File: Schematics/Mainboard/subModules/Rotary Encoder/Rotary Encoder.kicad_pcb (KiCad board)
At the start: 2 copper layers, 22.1 x 22.1 mm, 7 parts, among them J1 Power, J2 Data, SW1 Rot

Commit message: Moved F.Fab
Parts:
- moved R1 16.8 mm to (134.6, 107.7), turned to 90 degrees
- moved J2 16.1 mm to (155.7, 98.9), turned to 0 degrees
- moved J1 16.0 mm to (133.6, 104.0), turned to 180 degrees
- moved R2 14.8 mm to (136.4, 107.7), turned to 90 degrees
- moved R3 14.4 mm to (136.4, 95.0), turned to -90 degrees
- moved C1 11.5 mm to (136.4, 101.3), turned to 90 degrees
- moved SW1 11.3 mm to (142.2, 108.7), turned to 90 degrees

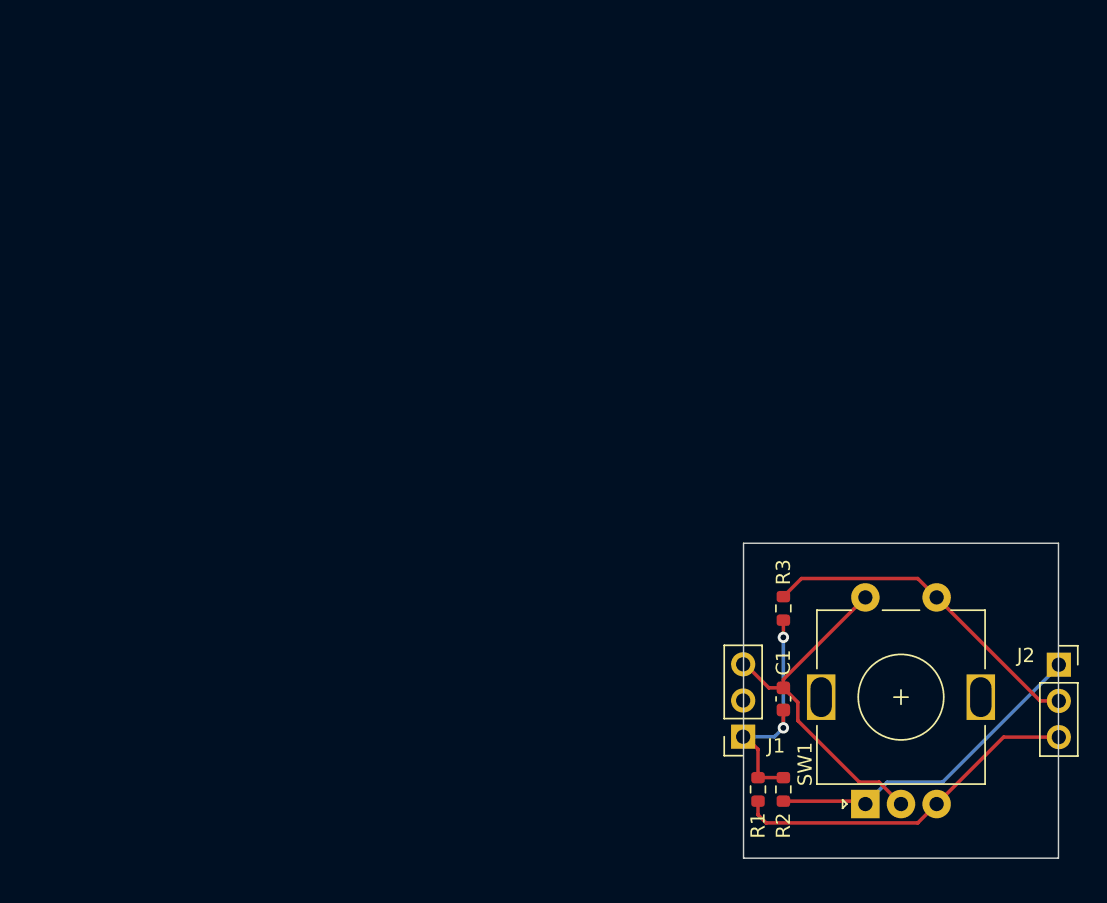
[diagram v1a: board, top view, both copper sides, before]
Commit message: rotated export pins
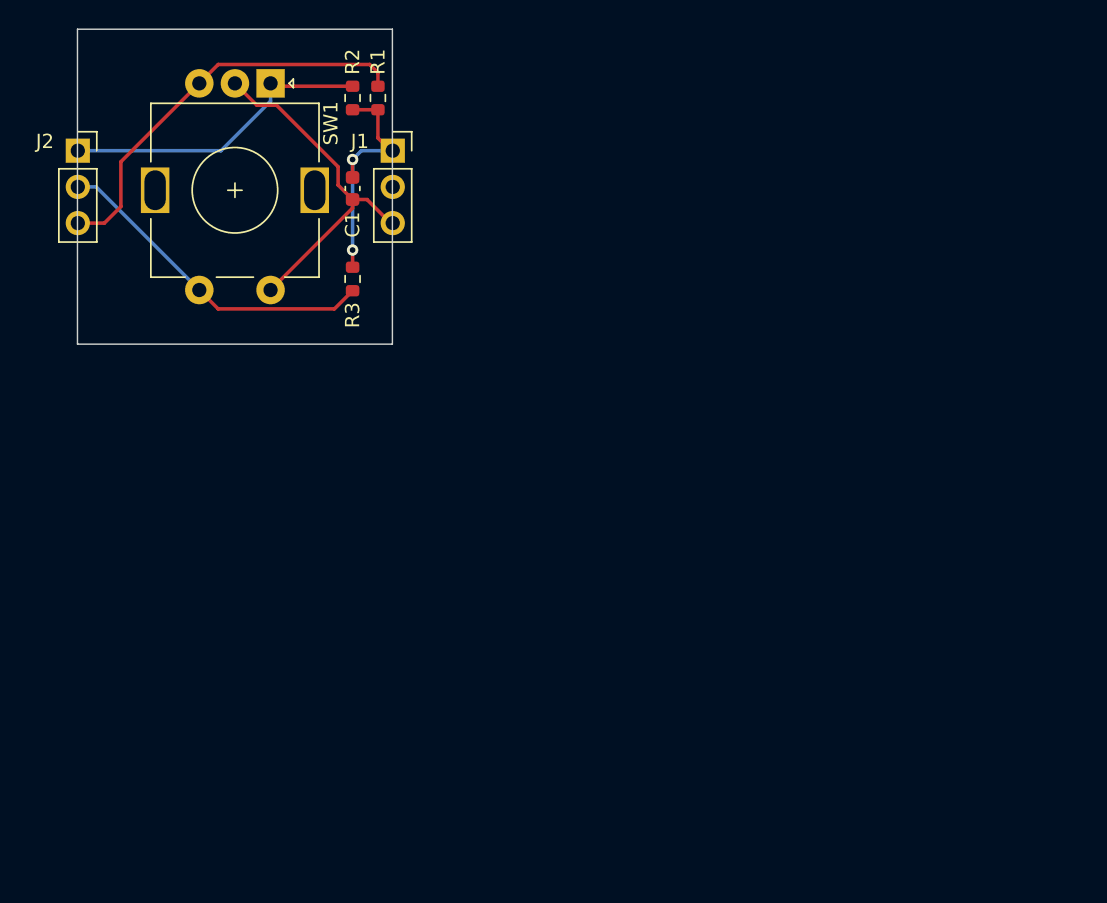
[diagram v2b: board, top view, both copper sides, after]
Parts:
- moved J2 77.7 mm to (86.9, 62.9)
- moved SW1 65.6 mm to (100.4, 58.2), turned to -90 degrees
- moved R2 57.2 mm to (106.2, 59.2), turned to -90 degrees
- moved R1 55.4 mm to (108.0, 59.2), turned to -90 degrees
- moved J1 47.9 mm to (109.0, 62.9), turned to 0 degrees
- moved C1 46.9 mm to (106.2, 65.5), turned to -90 degrees
- moved R3 38.1 mm to (106.2, 71.9), turned to 90 degrees
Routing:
- net /B: track 24.6 -> 28.6 mm
- net /A: track 23.5 -> 22.0 mm
